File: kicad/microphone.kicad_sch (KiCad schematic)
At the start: 20 parts, among them J1 Conn_01x02_Male, J2 Conn_01x02_Male, Q1 Q_NJFET_SDG, U1 OPA322S

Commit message: Updated passive footprints to 0805s
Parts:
- C1, C2, C3, C5, C6, C7, C8: footprint (none) -> Capacitor_SMD:C_0805_2012Metric
- R1, R2, R3, R4, R5, R6, R7, R8: footprint (none) -> Resistor_SMD:R_0805_2012Metric
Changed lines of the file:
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@@
       (effects (font (size 1.27 1.27)) (justify left))
     )
-    (property "Footprint" "" (id 2) (at 101.6 85.725 0)
+    (property "Footprint" "Resistor_SMD:R_0805_2012Metric" (id 2) (at 101.6 85.725 0)
       (effects (font (size 1.27 1.27)) hide)
     )
@@
       (effects (font (size 1.27 1.27)) (justify left))
     )
-    (property "Footprint" "" (id 2) (at 156.21 85.725 0)
+    (property "Footprint" "Resistor_SMD:R_0805_2012Metric" (id 2) (at 156.21 85.725 0)
       (effects (font (size 1.27 1.27)) hide)
     )
@@
       (effects (font (size 1.27 1.27)) (justify left))
     )
-    (property "Footprint" "" (id 2) (at 147.32 138.43 0)
+    (property "Footprint" "Resistor_SMD:R_0805_2012Metric" (id 2) (at 147.32 138.43 0)
       (effects (font (size 1.27 1.27)) hide)
     )
@@
     (property "Reference" "C7" (id 0) (at 166.37 143.51 0))
     (property "Value" "0.1uF" (id 1) (at 167.64 145.415 0))
-    (property "Footprint" "" (id 2) (at 162.56 144.145 0)
+    (property "Footprint" "Capacitor_SMD:C_0805_2012Metric" (id 2) (at 162.56 144.145 0)
       (effects (font (size 1.27 1.27)) hide)
     )
@@
     (property "Reference" "C3" (id 0) (at 112.395 90.805 90))
     (property "Value" "4.3uF" (id 1) (at 112.395 97.155 90))
-    (property "Footprint" "" (id 2) (at 112.395 93.98 0)
+    (property "Footprint" "Capacitor_SMD:C_0805_2012Metric" (id 2) (at 112.395 93.98 0)
       (effects (font (size 1.27 1.27)) hide)
     )
@@
       (effects (font (size 1.27 1.27)) (justify left))
     )
-    (property "Footprint" "" (id 2) (at 197.485 106.045 0)
+    (property "Footprint" "Resistor_SMD:R_0805_2012Metric" (id 2) (at 197.485 106.045 0)
       (effects (font (size 1.27 1.27)) hide)
     )
@@
     (property "Reference" "C5" (id 0) (at 190.5 93.345 90))
     (property "Value" "3uF" (id 1) (at 190.5 99.695 90))
-    (property "Footprint" "" (id 2) (at 190.5 96.52 0)
+    (property "Footprint" "Capacitor_SMD:C_0805_2012Metric" (id 2) (at 190.5 96.52 0)
       (effects (font (size 1.27 1.27)) hide)
     )
@@
     (property "Reference" "C8" (id 0) (at 176.53 143.51 0))
     (property "Value" "100nF" (id 1) (at 178.435 145.415 0))
-    (property "Footprint" "" (id 2) (at 172.72 144.145 0)
+    (property "Footprint" "Capacitor_SMD:C_0805_2012Metric" (id 2) (at 172.72 144.145 0)
       (effects (font (size 1.27 1.27)) hide)
     )
@@
     (property "Reference" "C2" (id 0) (at 156.21 74.295 90))
     (property "Value" "6.8pF" (id 1) (at 156.845 80.645 90))
-    (property "Footprint" "" (id 2) (at 156.21 77.47 0)
+    (property "Footprint" "Capacitor_SMD:C_0805_2012Metric" (id 2) (at 156.21 77.47 0)
       (effects (font (size 1.27 1.27)) hide)
     )
@@
       (effects (font (size 1.27 1.27)) (justify left))
     )
-    (property "Footprint" "" (id 2) (at 101.6 116.84 0)
+    (property "Footprint" "Resistor_SMD:R_0805_2012Metric" (id 2) (at 101.6 116.84 0)
       (effects (font (size 1.27 1.27)) hide)
     )
@@
     (property "Reference" "C1" (id 0) (at 129.54 151.13 0))
     (property "Value" "4.3uF" (id 1) (at 130.81 153.035 0))
-    (property "Footprint" "" (id 2) (at 125.73 151.765 0)
+    (property "Footprint" "Capacitor_SMD:C_0805_2012Metric" (id 2) (at 125.73 151.765 0)
       (effects (font (size 1.27 1.27)) hide)
     )
@@
       (effects (font (size 1.27 1.27)) (justify left))
     )
-    (property "Footprint" "" (id 2) (at 120.015 111.76 0)
+    (property "Footprint" "Resistor_SMD:R_0805_2012Metric" (id 2) (at 120.015 111.76 0)
       (effects (font (size 1.27 1.27)) hide)
     )
@@
       (effects (font (size 1.27 1.27)) (justify left))
     )
-    (property "Footprint" "" (id 2) (at 120.015 122.555 0)
+    (property "Footprint" "Resistor_SMD:R_0805_2012Metric" (id 2) (at 120.015 122.555 0)
       (effects (font (size 1.27 1.27)) hide)
     )
@@
       (effects (font (size 1.27 1.27)) (justify left))
     )
-    (property "Footprint" "" (id 2) (at 181.61 96.52 0)
+    (property "Footprint" "Resistor_SMD:R_0805_2012Metric" (id 2) (at 181.61 96.52 0)
       (effects (font (size 1.27 1.27)) hide)
     )
@@
     (property "Reference" "C6" (id 0) (at 131.445 121.92 0))
     (property "Value" "3uF" (id 1) (at 132.08 123.825 0))
-    (property "Footprint" "" (id 2) (at 127.635 122.555 0)
+    (property "Footprint" "Capacitor_SMD:C_0805_2012Metric" (id 2) (at 127.635 122.555 0)
       (effects (font (size 1.27 1.27)) hide)
     )
@@
     )
     (path "/d83ddfb8-6eb4-47cb-8f22-bf6073a6c32a"
-      (reference "C1") (unit 1) (value "4.3uF") (footprint "")
+      (reference "C1") (unit 1) (value "4.3uF") (footprint "Capacitor_SMD:C_0805_2012Metric")
     )
     (path "/d4fd7b8e-b219-4a81-93e4-4cd60969d29b"
-      (reference "C2") (unit 1) (value "6.8pF") (footprint "")
+      (reference "C2") (unit 1) (value "6.8pF") (footprint "Capacitor_SMD:C_0805_2012Metric")
     )
     (path "/9f811b9b-3190-4c8e-ad88-9b4bde6db61d"
-      (reference "C3") (unit 1) (value "4.3uF") (footprint "")
+      (reference "C3") (unit 1) (value "4.3uF") (footprint "Capacitor_SMD:C_0805_2012Metric")
     )
     (path "/b52d3101-479f-460f-9e74-2f7ce5d3142b"
-      (reference "C5") (unit 1) (value "3uF") (footprint "")
+      (reference "C5") (unit 1) (value "3uF") (footprint "Capacitor_SMD:C_0805_2012Metric")
     )
     (path "/fb06a837-f9bf-4bc1-b3eb-921df66b27b9"
-      (reference "C6") (unit 1) (value "3uF") (footprint "")
+      (reference "C6") (unit 1) (value "3uF") (footprint "Capacitor_SMD:C_0805_2012Metric")
     )
     (path "/8b9da899-a4a4-4a6d-b9f6-f8b071aa037a"
-      (reference "C7") (unit 1) (value "0.1uF") (footprint "")
+      (reference "C7") (unit 1) (value "0.1uF") (footprint "Capacitor_SMD:C_0805_2012Metric")
     )
     (path "/c2c2e8ec-c80a-49b4-b952-7e31c70a9df1"
-      (reference "C8") (unit 1) (value "100nF") (footprint "")
+      (reference "C8") (unit 1) (value "100nF") (footprint "Capacitor_SMD:C_0805_2012Metric")
     )
     (path "/13725934-af02-4eba-89d8-2bfe50c2ce66"
@@
     )
     (path "/54bf94d5-9aa3-4442-b1c7-bbbdd1385e7c"
-      (reference "R1") (unit 1) (value "6.98K") (footprint "")
+      (reference "R1") (unit 1) (value "6.98K") (footprint "Resistor_SMD:R_0805_2012Metric")
     )
     (path "/6f70bbb6-bbd6-4989-9831-57aa0b22fb1a"
-      (reference "R2") (unit 1) (value "169K") (footprint "")
+      (reference "R2") (unit 1) (value "169K") (footprint "Resistor_SMD:R_0805_2012Metric")
     )
     (path "/f1a7e9a3-6853-4046-a22f-32405eba4f35"
-      (reference "R3") (unit 1) (value "100K") (footprint "")
+      (reference "R3") (unit 1) (value "100K") (footprint "Resistor_SMD:R_0805_2012Metric")
     )
     (path "/f63fd2d0-0b05-4a4e-8bc8-d9cb737bd221"
-      (reference "R4") (unit 1) (value "49.9") (footprint "")
+      (reference "R4") (unit 1) (value "49.9") (footprint "Resistor_SMD:R_0805_2012Metric")
     )
     (path "/f2a3cf8c-927f-4ab8-b93e-0f53fea3f540"
-      (reference "R5") (unit 1) (value "100K") (footprint "")
+      (reference "R5") (unit 1) (value "100K") (footprint "Resistor_SMD:R_0805_2012Metric")
     )
     (path "/a3a39ddf-23a2-44ee-8bc1-685331d64cb1"
-      (reference "R6") (unit 1) (value "100K") (footprint "")
+      (reference "R6") (unit 1) (value "100K") (footprint "Resistor_SMD:R_0805_2012Metric")
     )
     (path "/d6c0ece7-ca23-4878-862b-ada2d307c5c2"
-      (reference "R7") (unit 1) (value "2.2K") (footprint "")
+      (reference "R7") (unit 1) (value "2.2K") (footprint "Resistor_SMD:R_0805_2012Metric")
     )
     (path "/7cbf4520-9b5c-4aef-ac0a-9633aa014dd9"
-      (reference "R8") (unit 1) (value "0") (footprint "")
+      (reference "R8") (unit 1) (value "0") (footprint "Resistor_SMD:R_0805_2012Metric")
     )
     (path "/3a2bf432-24ca-46a8-9644-15037ac2e51b"

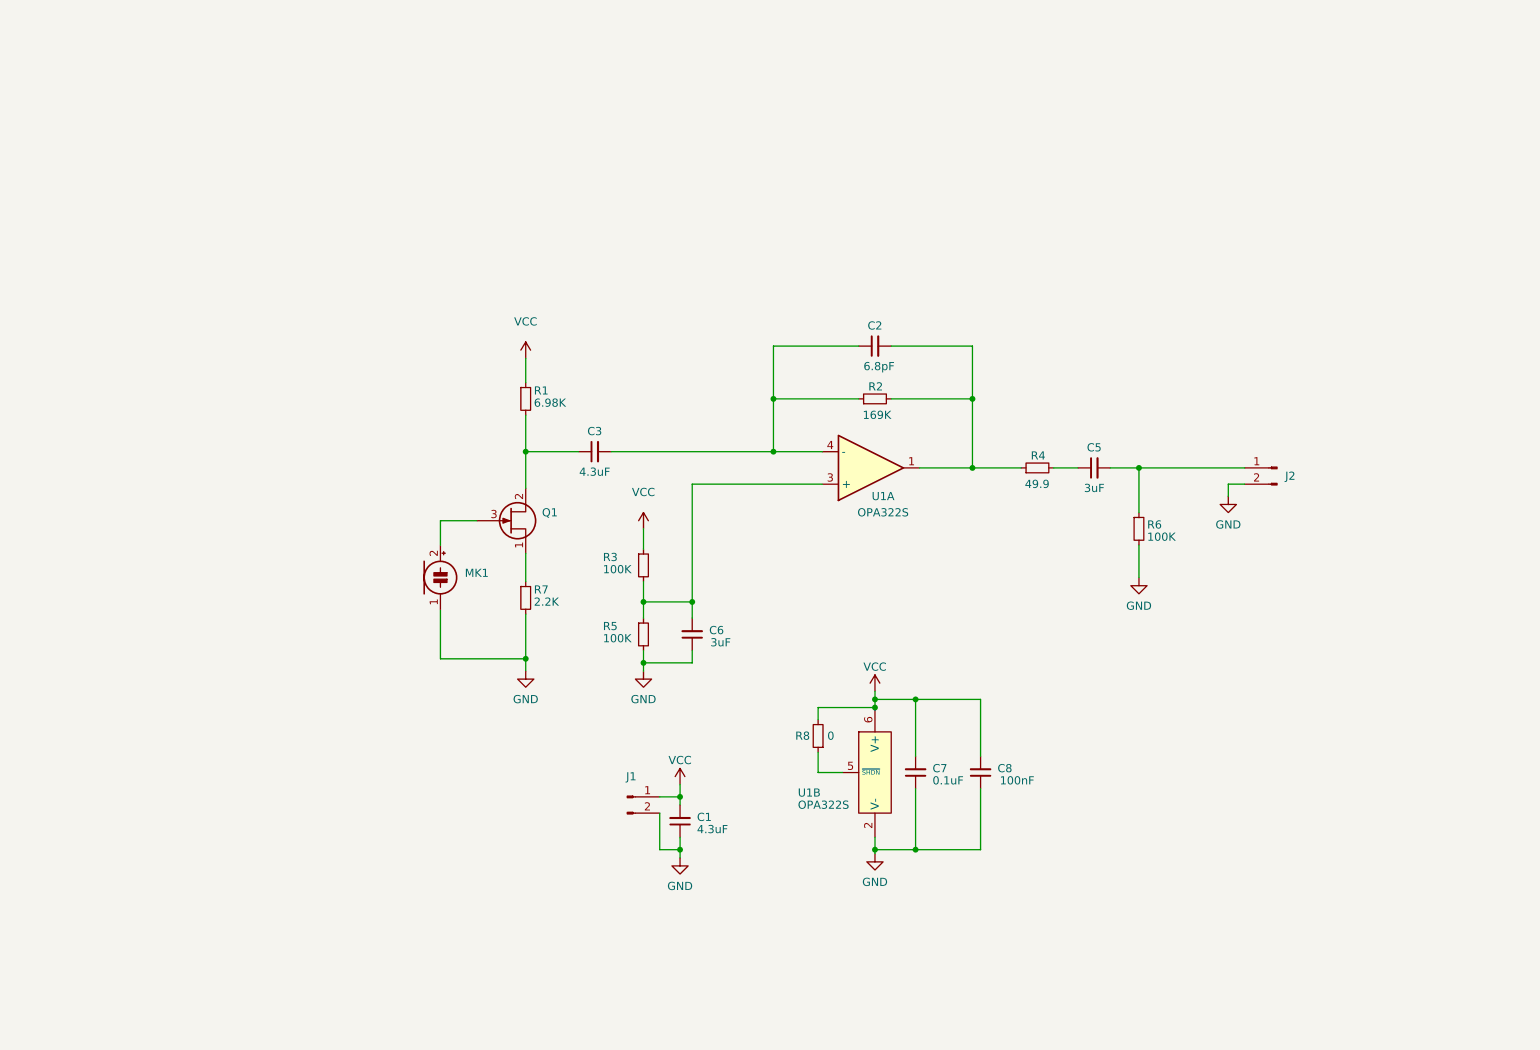
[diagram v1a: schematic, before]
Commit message: merging in changes in schematic + adding sim for dual gain stages
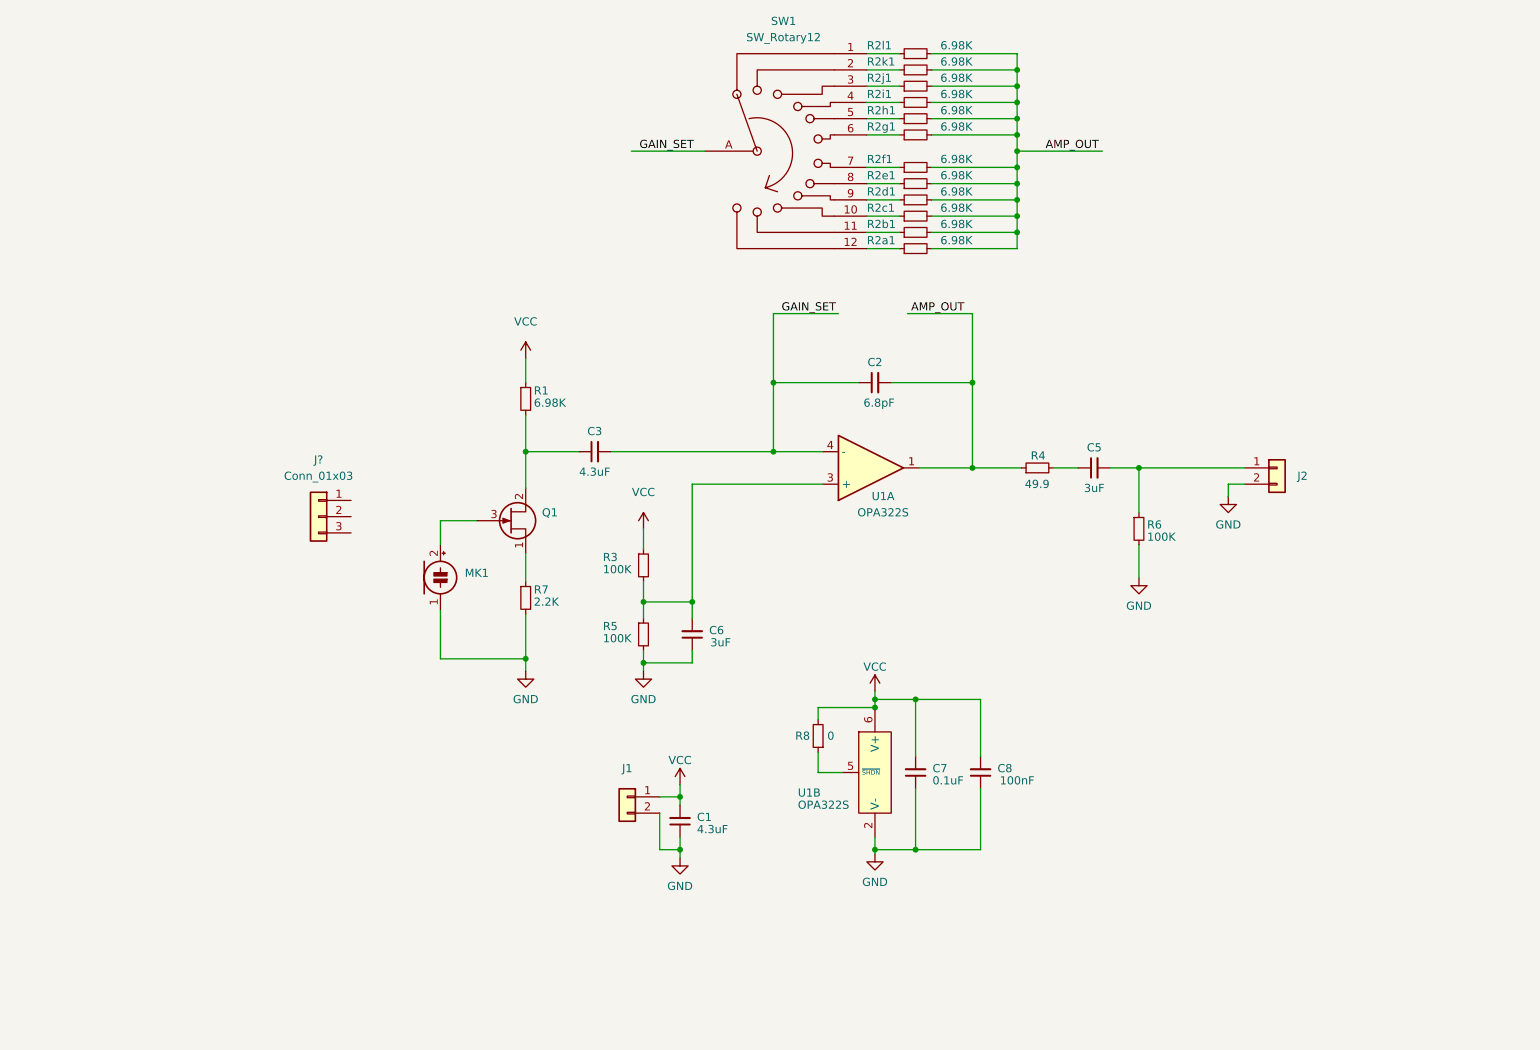
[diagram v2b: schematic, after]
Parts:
- removed R2: 169K, Resistor_SMD:R_0805_2012Metric, symbol Device:R_Small
- added J?: Conn_01x03, symbol Connector_Generic:Conn_01x03
- added R2a1, R2b1, R2c1, R2d1, R2e1, R2f1, R2g1, R2h1, R2i1, R2j1, R2k1, R2l1: 6.98K, Resistor_SMD:R_0805_2012Metric, symbol Device:R_Small
- added SW1: SW_Rotary12, Capacitor_SMD:C_0805_2012Metric, symbol Switch:SW_Rotary12
- J1, J2: symbol Connector:Conn_01x02_Male -> Connector_Generic:Conn_01x02
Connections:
- net AMP_OUT: now reaches C2.2, R4.1, U1.1
- net AMP_OUT: now also R2a1.2, R2b1.2, R2c1.2, R2d1.2, R2e1.2, R2f1.2, R2g1.2, R2h1.2, R2i1.2, R2j1.2, R2k1.2, R2l1.2
- net GAIN_SET: now reaches C2.1, C3.2, U1.4 (-)
- net GAIN_SET: now also SW1.A
- new net: R2d1.1, SW1.9
- new net: R2c1.1, SW1.10
- new net: R2i1.1, SW1.4
- new net: R2b1.1, SW1.11
- new net: R2g1.1, SW1.6
- new net: R2a1.1, SW1.12
- new net: R2k1.1, SW1.2
- new net: R2f1.1, SW1.7
- new net: R2j1.1, SW1.3
- new net: R2l1.1, SW1.1
- new net: R2h1.1, SW1.5
- new net: R2e1.1, SW1.8
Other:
- moved on the sheet: C2

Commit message: starting 2 stage amp design
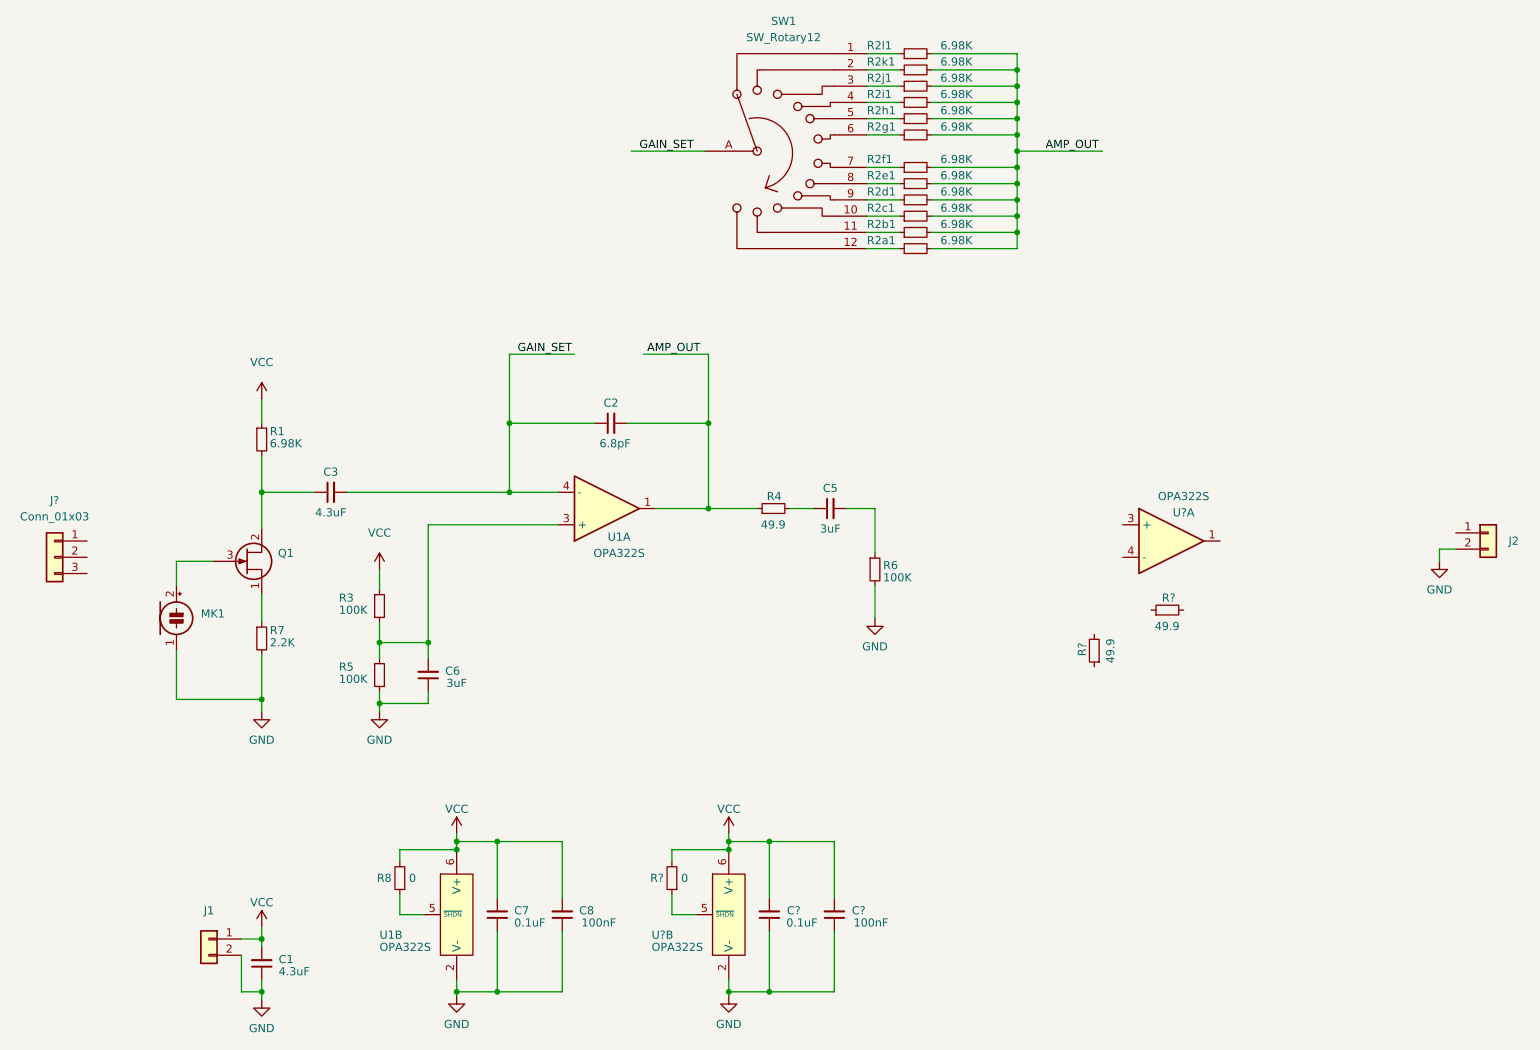
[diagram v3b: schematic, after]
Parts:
- added C?: 100nF, Capacitor_SMD:C_0805_2012Metric, symbol Device:C_Small
- added C?: 0.1uF, Capacitor_SMD:C_0805_2012Metric, symbol Device:C_Small
- added R? (x2): 49.9, Resistor_SMD:R_0805_2012Metric, symbol Device:R_Small
- added R?: 0, Resistor_SMD:R_0805_2012Metric, symbol Device:R_Small
- added U? (x2): OPA322S, Package_TO_SOT_SMD:SOT-23-6, symbol Project_Lib:OPA322S
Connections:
- net GND: now also C?.1, C?.1, U?.2 (V-)
- net VCC: now also C?.2, C?.2, R?.2, U?.6 (V+)
- net at C5.2, R6.1: no longer J2.1 (Pin_1)
- new net: R?.1, U?.5 (~{SHDN})
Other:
- moved on the sheet: C1, C2, C3, C5, C6, C7, C8, J1, J2, J?, MK1, Q1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
